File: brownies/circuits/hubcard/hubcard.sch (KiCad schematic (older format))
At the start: 12 parts, among them J1 Conn_02x10_Odd_Even, J2 Conn_02x04_Odd_Even, J3 Conn_01x03_Male, J4 Conn_01x04_Male, Q1 IRF5305, U1 ATtiny85V-10PU

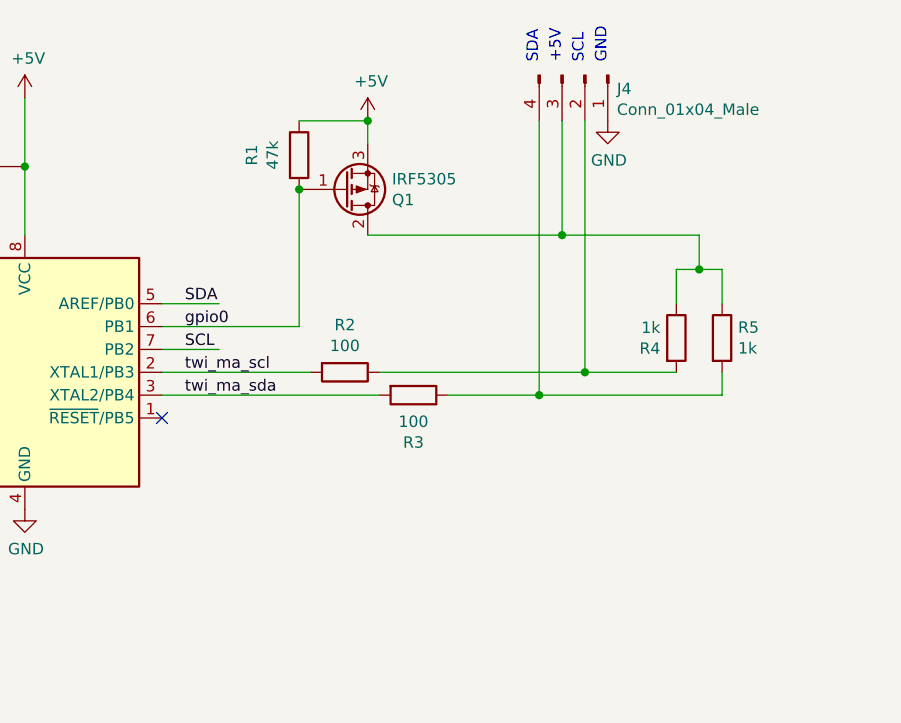
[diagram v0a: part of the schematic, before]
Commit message: Add MQTT gateway driver; Add rain warning to weather driver; Improve floor plan UI; Many minor improvements
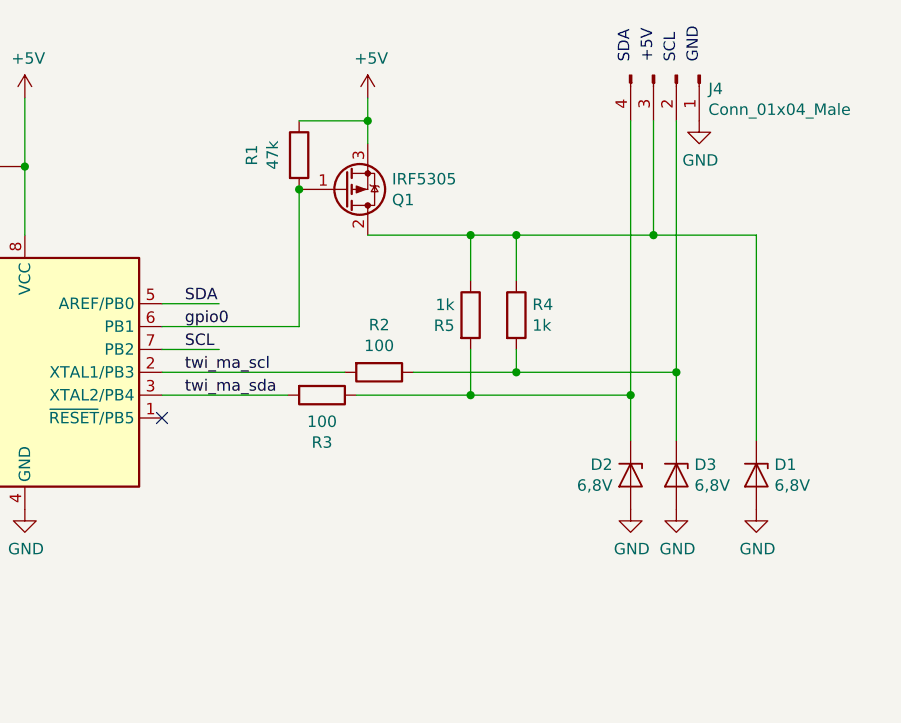
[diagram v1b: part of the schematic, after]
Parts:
- added D1, D2, D3: 6,8V, Diode_THT:D_DO-34_SOD68_P7.62mm_Horizontal, symbol Device:D_Zener
- renumbered R5 to R4, R4 to R5
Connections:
- wire segments 45 -> 49
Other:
- moved on the sheet: J4, R2, R3, R4, R5
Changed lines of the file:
@@
 encoding utf-8
 Sheet 1 1
-Title "Asterix Hub Card"
-Date "2019-07-14"
+Title "Root Hub Card"
+Date "2020-05-15"
 Rev ""
 Comp "Gundolf Kiefer"
@@
 Wire Wire Line
 	3550 2600 3550 2900
-Wire Wire Line
-	3550 2300 3550 2600
-Connection ~ 3550 2600
 $Comp
 L Transistor_FET:IRF4905 Q1
@@
 L power:+5V #PWR0108
 U 1 1 5D2B3ED0
-P 5050 2400
-F 0 "#PWR0108" H 5050 2250 50  0001 C CNN
-F 1 "+5V" H 5065 2573 50  0000 C CNN
-F 2 "" H 5050 2400 50  0001 C CNN
-F 3 "" H 5050 2400 50  0001 C CNN
-	1    5050 2400
+P 5050 2300
+F 0 "#PWR0108" H 5050 2150 50  0001 C CNN
+F 1 "+5V" H 5065 2473 50  0000 C CNN
+F 2 "" H 5050 2300 50  0001 C CNN
+F 3 "" H 5050 2300 50  0001 C CNN
+	1    5050 2300
 	1    0    0    -1
 $EndComp
@@
 Wire Wire Line
 	5050 2400 5050 2500
-Connection ~ 5050 2400
 Wire Wire Line
 	4750 2700 4750 3300
@@
 L Connector:Conn_01x04_Male J4
 U 1 1 5D2B47CB
-P 6000 2200
-F 0 "J4" V 6060 2340 50  0000 L CNN
-F 1 "Conn_01x04_Male" V 6151 2340 50  0000 L CNN
-F 2 "kicad-library:PinHeader_1x04_Home2lBus" H 6000 2200 50  0001 C CNN
-F 3 "~" H 6000 2200 50  0001 C CNN
-	1    6000 2200
-	0    1    1    0
-$EndComp
-Wire Wire Line
-	5050 2900 5900 2900
-Wire Wire Line
-	5900 2900 5900 2400
+P 6400 2200
+F 0 "J4" V 6460 2340 50  0000 L CNN
+F 1 "Conn_01x04_Male" V 6551 2340 50  0000 L CNN
+F 2 "kicad-library:PinHeader_1x04_Home2lBus" H 6400 2200 50  0001 C CNN
+F 3 "~" H 6400 2200 50  0001 C CNN
+	1    6400 2200
+	0    1    1    0
+$EndComp
+Wire Wire Line
+	6300 2900 6300 2400
 $Comp
 L power:GND #PWR0109
 U 1 1 5D2B4A21
-P 6100 2400
-F 0 "#PWR0109" H 6100 2150 50  0001 C CNN
-F 1 "GND" H 6105 2227 50  0000 C CNN
-F 2 "" H 6100 2400 50  0001 C CNN
-F 3 "" H 6100 2400 50  0001 C CNN
-	1    6100 2400
+P 6500 2400
+F 0 "#PWR0109" H 6500 2150 50  0001 C CNN
+F 1 "GND" H 6505 2227 50  0000 C CNN
+F 2 "" H 6500 2400 50  0001 C CNN
+F 3 "" H 6500 2400 50  0001 C CNN
+	1    6500 2400
 	1    0    0    -1
 $EndComp
@@
 L Device:R R2
 U 1 1 5D2B4FF4
-P 4950 3500
-F 0 "R2" V 4743 3500 50  0000 C CNN
-F 1 "100" V 4834 3500 50  0000 C CNN
-F 2 "Resistor_THT:R_Axial_DIN0207_L6.3mm_D2.5mm_P7.62mm_Horizontal" V 4880 3500 50  0001 C CNN
-F 3 "~" H 4950 3500 50  0001 C CNN
-	1    4950 3500
-	0    1    1    0
-$EndComp
-$Comp
-L Device:R R3
-U 1 1 5D2B50A9
-P 5250 3600
-F 0 "R3" V 5457 3600 50  0000 C CNN
-F 1 "100" V 5366 3600 50  0000 C CNN
-F 2 "Resistor_THT:R_Axial_DIN0207_L6.3mm_D2.5mm_P7.62mm_Horizontal" V 5180 3600 50  0001 C CNN
-F 3 "~" H 5250 3600 50  0001 C CNN
-	1    5250 3600
+P 5100 3500
+F 0 "R2" V 4893 3500 50  0000 C CNN
+F 1 "100" V 4984 3500 50  0000 C CNN
+F 2 "Resistor_THT:R_Axial_DIN0207_L6.3mm_D2.5mm_P7.62mm_Horizontal" V 5030 3500 50  0001 C CNN
+F 3 "~" H 5100 3500 50  0001 C CNN
+	1    5100 3500
 	0    1    1    0
 $EndComp
@@
 twi_ma_sda
 $Comp
+L Device:R R5
+U 1 1 5D2B57DB
+P 5500 3250
+F 0 "R5" H 5430 3204 50  0000 R CNN
+F 1 "1k" H 5430 3295 50  0000 R CNN
+F 2 "Resistor_THT:R_Axial_DIN0207_L6.3mm_D2.5mm_P7.62mm_Horizontal" V 5430 3250 50  0001 C CNN
+F 3 "~" H 5500 3250 50  0001 C CNN
+	1    5500 3250
+	1    0    0    -1
+$EndComp
+$Comp
 L Device:R R4
-U 1 1 5D2B57DB
-P 6400 3350
-F 0 "R4" H 6330 3304 50  0000 R CNN
-F 1 "1k" H 6330 3395 50  0000 R CNN
-F 2 "Resistor_THT:R_Axial_DIN0207_L6.3mm_D2.5mm_P7.62mm_Horizontal" V 6330 3350 50  0001 C CNN
-F 3 "~" H 6400 3350 50  0001 C CNN
-	1    6400 3350
-	1    0    0    -1
-$EndComp
-$Comp
-L Device:R R5
 U 1 1 5D2B589C
-P 6600 3350
-F 0 "R5" H 6670 3396 50  0000 L CNN
-F 1 "1k" H 6670 3305 50  0000 L CNN
-F 2 "Resistor_THT:R_Axial_DIN0207_L6.3mm_D2.5mm_P7.62mm_Horizontal" V 6530 3350 50  0001 C CNN
-F 3 "~" H 6600 3350 50  0001 C CNN
-	1    6600 3350
-	1    0    0    -1
-$EndComp
-Wire Wire Line
-	5100 3500 6000 3500
-Connection ~ 6000 3500
-Wire Wire Line
-	6000 3500 6400 3500
-Wire Wire Line
-	4150 3600 5100 3600
-Wire Wire Line
-	5400 3600 5800 3600
-Wire Wire Line
-	6600 3600 6600 3500
-Wire Wire Line
-	6000 3500 6000 2400
-Wire Wire Line
-	4150 3500 4800 3500
-Wire Wire Line
-	5800 2400 5800 3600
-Connection ~ 5800 3600
-Wire Wire Line
-	5800 3600 6600 3600
-Text Notes 5800 2150 1    50   ~ 0
+P 5700 3250
+F 0 "R4" H 5770 3296 50  0000 L CNN
+F 1 "1k" H 5770 3205 50  0000 L CNN
+F 2 "Resistor_THT:R_Axial_DIN0207_L6.3mm_D2.5mm_P7.62mm_Horizontal" V 5630 3250 50  0001 C CNN
+F 3 "~" H 5700 3250 50  0001 C CNN
+	1    5700 3250
+	1    0    0    -1
+$EndComp
+Text Notes 6200 2150 1    50   ~ 0
 SDA
-Text Notes 5900 2150 1    50   ~ 0
+Text Notes 6300 2150 1    50   ~ 0
 +5V\n
-Text Notes 6000 2150 1    50   ~ 0
+Text Notes 6400 2150 1    50   ~ 0
 SCL\n
-Text Notes 6100 2150 1    50   ~ 0
+Text Notes 6500 2150 1    50   ~ 0
 GND
 Wire Wire Line
@@
 Connection ~ 3000 6500
 NoConn ~ 4150 3700
-Wire Wire Line
-	6400 3050 6400 3200
-Wire Wire Line
-	6600 3050 6600 3200
-Wire Wire Line
-	6400 3050 6500 3050
-Wire Wire Line
-	5900 2900 6500 2900
-Wire Wire Line
-	6500 2900 6500 3050
-Connection ~ 5900 2900
-Connection ~ 6500 3050
-Wire Wire Line
-	6500 3050 6600 3050
+$Comp
+L Device:D_Zener D1
+U 1 1 5EBE8A75
+P 6750 3950
+F 0 "D1" V 6704 4029 50  0000 L CNN
+F 1 "6,8V" V 6795 4029 50  0000 L CNN
+F 2 "Diode_THT:D_DO-34_SOD68_P7.62mm_Horizontal" H 6750 3950 50  0001 C CNN
+F 3 "~" H 6750 3950 50  0001 C CNN
+	1    6750 3950
+	0    1    1    0
+$EndComp
+$Comp
+L power:GND #PWR01
+U 1 1 5EBE8B9B
+P 6750 4100
+F 0 "#PWR01" H 6750 3850 50  0001 C CNN
+F 1 "GND" H 6755 3927 50  0000 C CNN
+F 2 "" H 6750 4100 50  0001 C CNN
+F 3 "" H 6750 4100 50  0001 C CNN
+	1    6750 4100
+	1    0    0    -1
+$EndComp
+$Comp
+L Device:D_Zener D2
+U 1 1 5EBE9D31
+P 6200 3950
+F 0 "D2" V 6154 3871 50  0000 R CNN
+F 1 "6,8V" V 6245 3871 50  0000 R CNN
+F 2 "Diode_THT:D_DO-34_SOD68_P7.62mm_Horizontal" H 6200 3950 50  0001 C CNN
+F 3 "~" H 6200 3950 50  0001 C CNN
+	1    6200 3950
+	0    1    1    0
+$EndComp
+$Comp
+L power:GND #PWR02
+U 1 1 5EBE9D38
+P 6200 4100
+F 0 "#PWR02" H 6200 3850 50  0001 C CNN
+F 1 "GND" H 6205 3927 50  0000 C CNN
+F 2 "" H 6200 4100 50  0001 C CNN
+F 3 "" H 6200 4100 50  0001 C CNN
+	1    6200 4100
+	1    0    0    -1
+$EndComp
+$Comp
+L Device:D_Zener D3
+U 1 1 5EBEA555
+P 6400 3950
+F 0 "D3" V 6354 4029 50  0000 L CNN
+F 1 "6,8V" V 6445 4029 50  0000 L CNN
+F 2 "Diode_THT:D_DO-34_SOD68_P7.62mm_Horizontal" H 6400 3950 50  0001 C CNN
+F 3 "~" H 6400 3950 50  0001 C CNN
+	1    6400 3950
+	0    1    1    0
+$EndComp
+$Comp
+L power:GND #PWR03
+U 1 1 5EBEA55C
+P 6400 4100
+F 0 "#PWR03" H 6400 3850 50  0001 C CNN
+F 1 "GND" H 6405 3927 50  0000 C CNN
+F 2 "" H 6400 4100 50  0001 C CNN
+F 3 "" H 6400 4100 50  0001 C CNN
+	1    6400 4100
+	1    0    0    -1
+$EndComp
+Wire Wire Line
+	6400 2400 6400 3500
+Wire Wire Line
+	5500 3100 5500 2900
+Wire Wire Line
+	5700 2900 6300 2900
+Wire Wire Line
+	5050 2900 5500 2900
+Wire Wire Line
+	5500 2900 5700 2900
+Connection ~ 5500 2900
+Connection ~ 5700 2900
+Wire Wire Line
+	6200 2400 6200 3600
+Wire Wire Line
+	5700 2900 5700 3100
+Wire Wire Line
+	5700 3400 5700 3500
+Connection ~ 5700 3500
+Wire Wire Line
+	5700 3500 6400 3500
+Wire Wire Line
+	5500 3400 5500 3600
+Wire Wire Line
+	5500 3600 6200 3600
+$Comp
+L Device:R R3
+U 1 1 5D2B50A9
+P 4850 3600
+F 0 "R3" V 5057 3600 50  0000 C CNN
+F 1 "100" V 4966 3600 50  0000 C CNN
+F 2 "Resistor_THT:R_Axial_DIN0207_L6.3mm_D2.5mm_P7.62mm_Horizontal" V 4780 3600 50  0001 C CNN
+F 3 "~" H 4850 3600 50  0001 C CNN
+	1    4850 3600
+	0    1    1    0
+$EndComp
+Wire Wire Line
+	5250 3500 5700 3500
+Wire Wire Line
+	4950 3500 4150 3500
+Wire Wire Line
+	4150 3600 4700 3600
+Wire Wire Line
+	5000 3600 5500 3600
+Connection ~ 5500 3600
+Wire Wire Line
+	6750 2900 6300 2900
+Connection ~ 6300 2900
+Connection ~ 3550 2600
+Wire Wire Line
+	3550 2300 3550 2600
+Wire Wire Line
+	5050 2300 5050 2400
+Connection ~ 5050 2400
+Wire Wire Line
+	6750 2900 6750 3800
+Wire Wire Line
+	6400 3800 6400 3500
+Connection ~ 6400 3500
+Wire Wire Line
+	6200 3800 6200 3600
+Connection ~ 6200 3600
 $EndSCHEMATC
